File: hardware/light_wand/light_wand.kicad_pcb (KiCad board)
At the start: 2 copper layers, 30.5 x 95.2 mm, 21 parts, among them J1 1x1 Conn, J2 1x1 Conn, J3 1x1 Conn, J4 1x1 Conn, J5 1x1 Conn, J6 1x1 Conn, U1 TLV61070A, U4 Pico

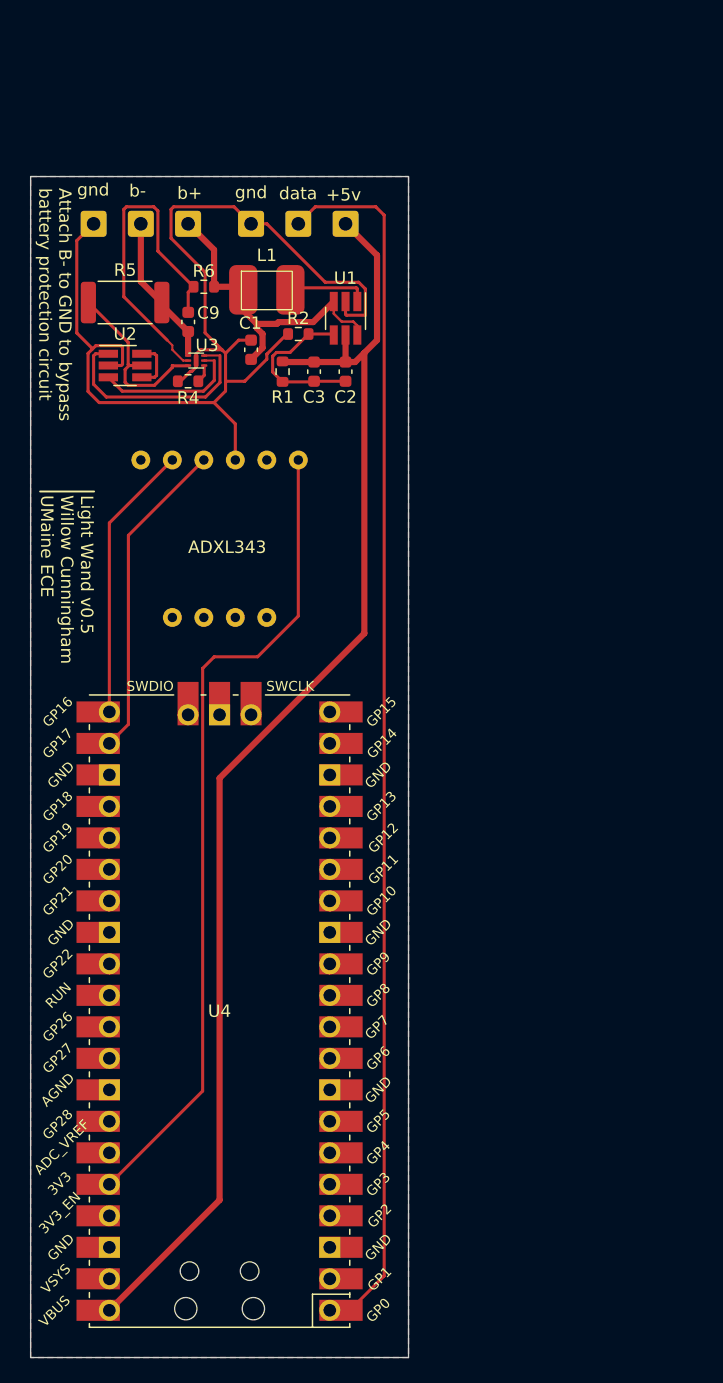
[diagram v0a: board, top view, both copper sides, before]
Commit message: Moved new components onto PCB
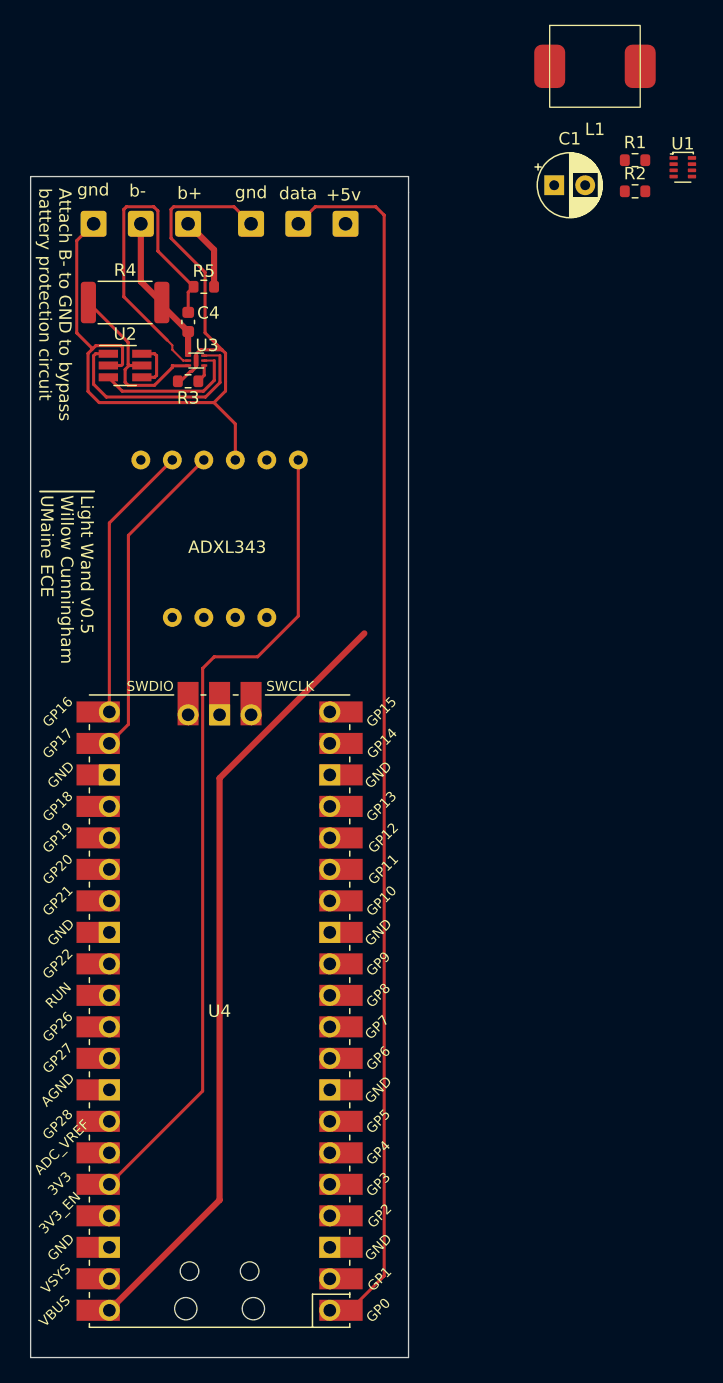
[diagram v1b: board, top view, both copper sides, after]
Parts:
- removed C2: 47uF, Capacitor_SMD:C_0603_1608Metric
- removed C3: 820pF, Capacitor_SMD:C_0603_1608Metric
- C1: value 10uF -> 100uF; footprint Capacitor_SMD:C_0603_1608Metric -> Capacitor_THT:CP_Radial_D5.0mm_P2.50mm
- L1: value 2.2uH -> .47uH; footprint light_wand_footprints:74438357022_4.1x3.1mm_Inductor -> light_wand_footprints:Inductor_SMD_L_7.3x7.3_H3.5
- R1: value 180k -> 110k
- R2: value 20k -> 15k
- U1: value TLV61070A -> TPS61033X; footprint Package_TO_SOT_SMD:SOT-23-6_Handsoldering -> Package_TO_SOT_SMD:SOT-583-8
- moved L1 34.6 mm to (170.0, 38.1)
- moved R1 33.2 mm to (173.2, 45.7), turned to 0 degrees
- moved U1 29.8 mm to (177.1, 46.2), turned to 0 degrees
- moved R2 29.5 mm to (173.2, 48.2), turned to 0 degrees
- moved C1 27.8 mm to (166.7, 47.7), turned to 0 degrees
- renumbered C9 to C4, R4 to R3, R5 to R4, R6 to R5
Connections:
- U1 pad 1: Net-(U1-SW) -> /Power Supply/Vin+
- U1 pad 2: GND -> /Power Supply/Vin+
- U1 pad 4: Net-(U1-FB) -> GND
- U1 pad 5: +5V -> Net-(U1-FB)
- U1 pad 6: /Power Supply/Vin+ -> GND
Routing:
- net +5V: track 106.7 -> 63.1 mm
- net GND: track 91.4 -> 65.9 mm
- net /Power Supply/Vin+: track 26.0 -> 5.95 mm
- net Net-(U1-FB): track 13.2 -> 0.00 mm
- net Net-(U1-SW): track 6.53 -> 0.00 mm
- removed copper zone on B.Cu, net GND
- removed copper zone on F.Cu, net GND

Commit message: Completed PCB laout
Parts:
- added C2: 10uF, Capacitor_SMD:C_0603_1608Metric, F.Cu at (145.4, 61.6)
- added C3: 10uF, Capacitor_SMD:C_0603_1608Metric, F.Cu at (150.1, 61.5)
- added C5: 10uF, Capacitor_SMD:C_0603_1608Metric, F.Cu at (151.9, 61.5)
- moved R1 33.0 mm to (147.0, 65.7)
- moved U1 32.9 mm to (147.8, 61.5)
- moved L1 30.8 mm to (144.8, 55.9)
- moved R2 29.2 mm to (148.7, 64.1)
- moved C1 28.4 mm to (142.5, 62.5), turned to 180 degrees
- moved C4 2.33 mm to (134.8, 58.7)
- moved R3 2.33 mm to (134.8, 63.5)
- moved R4 2.33 mm to (129.7, 57.1)
- moved R5 2.33 mm to (136.1, 55.9)
- moved U2 2.33 mm to (129.7, 62.2)
- moved U3 2.33 mm to (135.5, 61.8)
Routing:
- net GND: track 65.9 -> 125.1 mm, vias 0 -> 7
- net +5V: track 63.1 -> 105.4 mm, vias 0 -> 2
- net /Power Supply/Vin+: track 5.95 -> 22.8 mm
- net Net-(U1-SW): track 0.00 -> 6.12 mm
- net Net-(U1-FB): track 0.00 -> 3.74 mm
- net Net-(U3-VDD): track 27.1 -> 26.1 mm
- net Net-(J1-Pin_1): track 98.9 -> 99.4 mm
- net /Power Supply/Vin-: track 12.1 -> 11.6 mm
- added copper zone on F.Cu, net +5V
- added copper zone on F.Cu, net /Power Supply/Vin+
- added copper zone on F.Cu, net /Power Supply/Vin-
- added copper zone on B.Cu, net GND
- added copper zone on F.Cu, net GND
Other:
- board text added: "Attach B- to GND to bypass BMS"
- board text added: "Light Wand v1.0 Willow Cunningham UMaine ECE"
- board text removed: "Attach B- to GND to bypass battery protection circuit"
- board text removed: "Light Wand v0.5 Willow Cunningham UMaine ECE"
